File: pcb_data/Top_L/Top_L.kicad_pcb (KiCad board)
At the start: 2 copper layers, 134.5 x 96.4 mm, 42 parts, among them J1 Conn_01x02, U1 XIAO-nRF52840

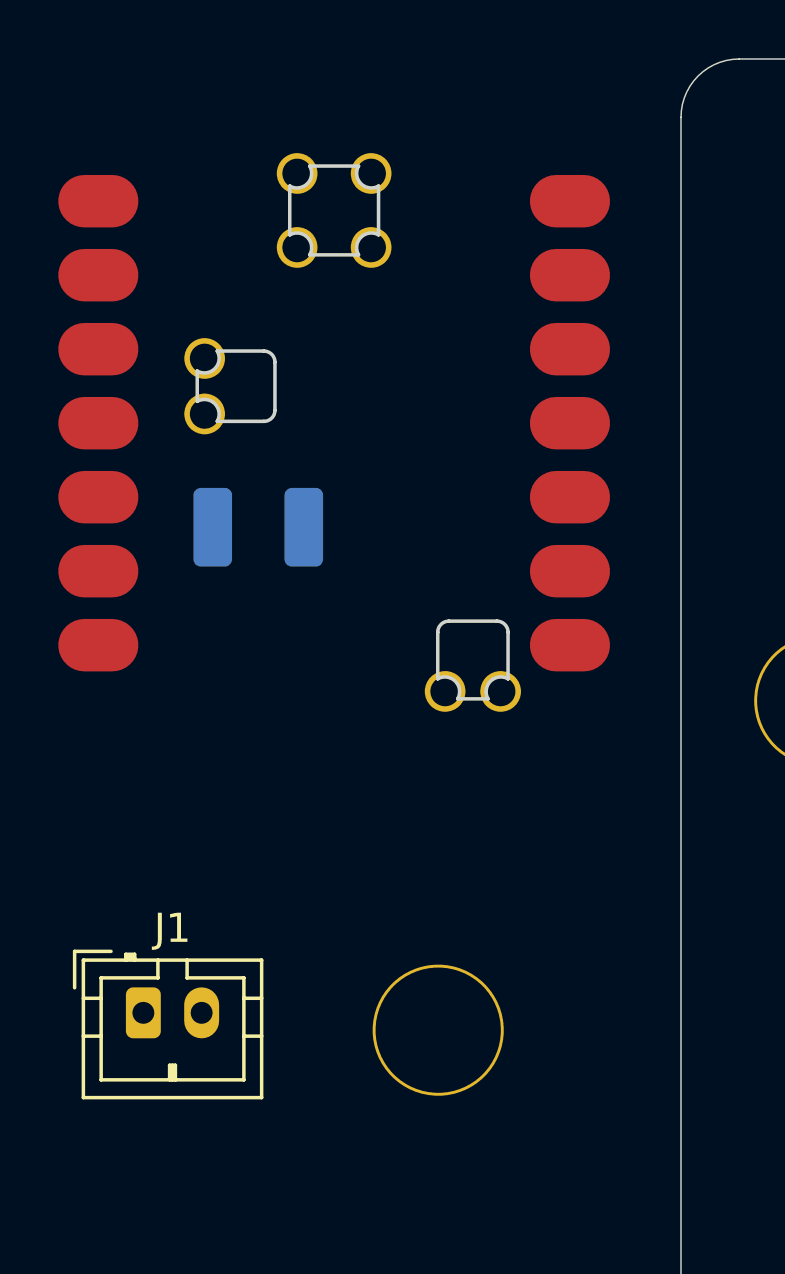
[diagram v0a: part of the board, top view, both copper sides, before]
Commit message: remove unnecessary footprint
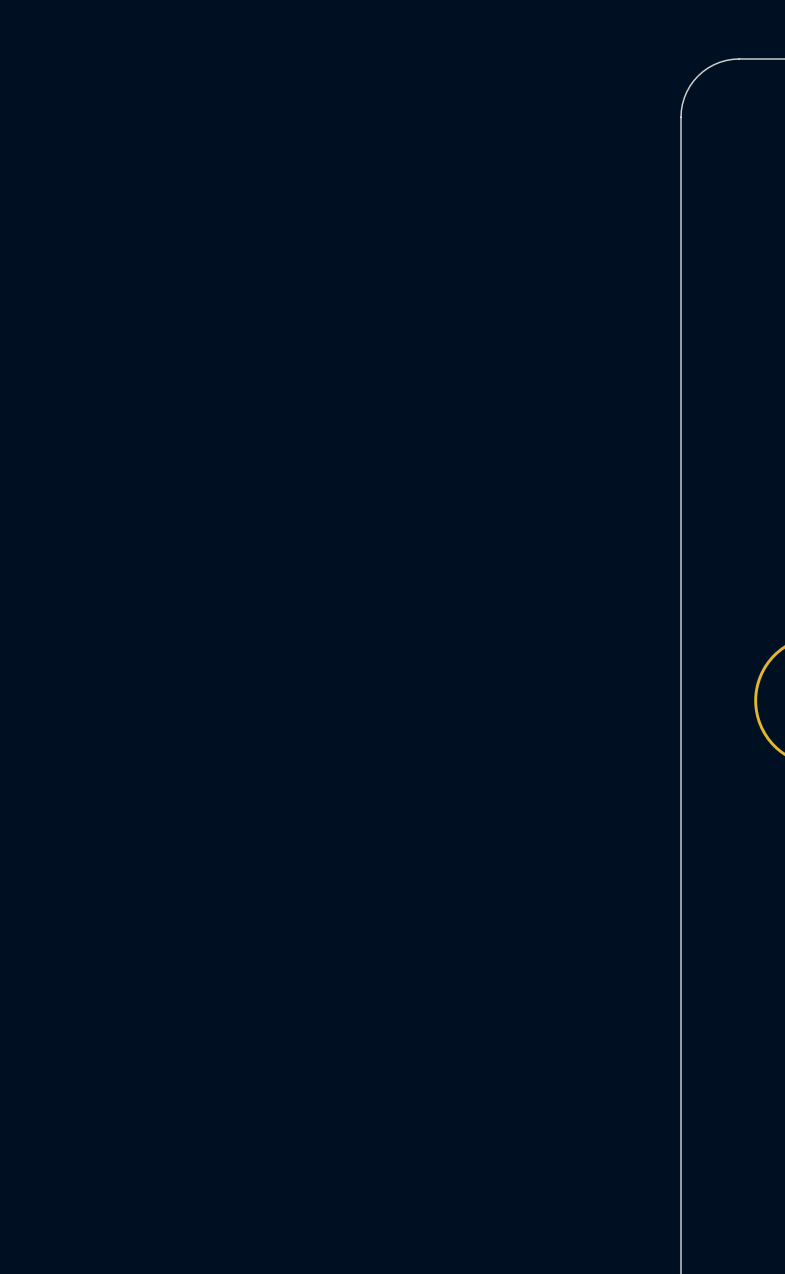
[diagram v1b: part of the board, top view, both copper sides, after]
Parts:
- removed C1: GRM32EC81C476KE15L, Capacitor_SMD:C_1210_3225Metric_Pad1.33x2.70mm_HandSolder
- removed H7: MountingHole, kbd_Hole:m2_Spacer_Hole
- removed J1: Conn_01x02, Connector_JST:JST_PH_B2B-PH-K_1x02_P2.00mm_Vertical
- removed U1: XIAO-nRF52840, mcu:xiao-ble-smd-cutout

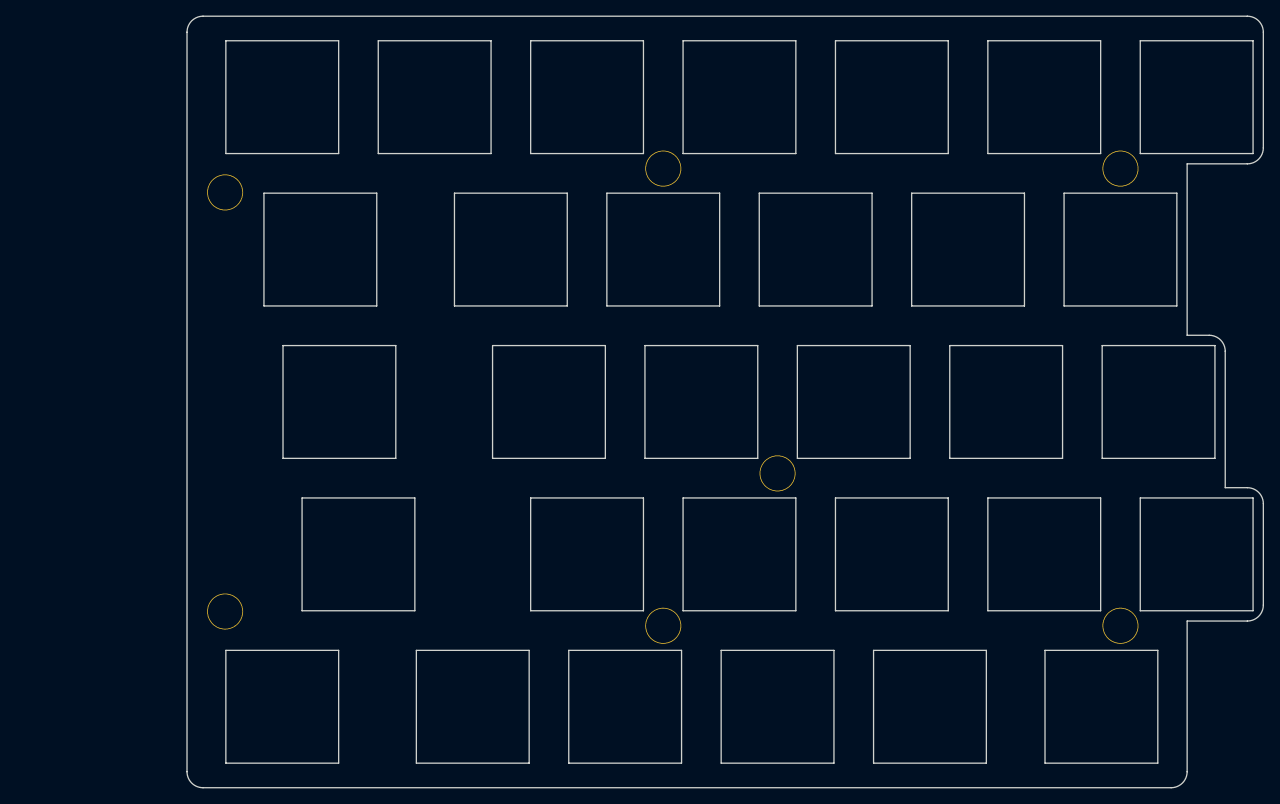
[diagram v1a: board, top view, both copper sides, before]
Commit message: fix hole footprint and number
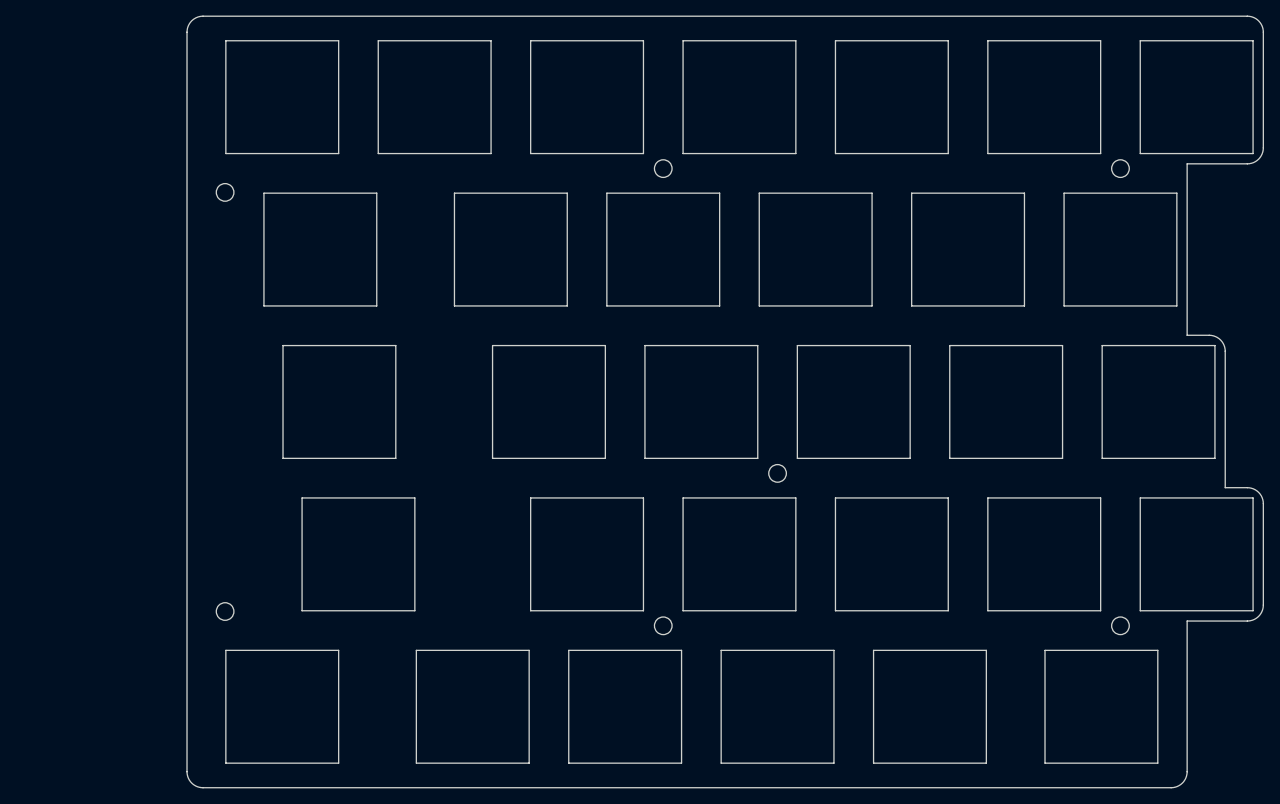
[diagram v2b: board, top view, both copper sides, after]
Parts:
- H1, H2, H3, H4, H5, H6: footprint kbd_Hole:m2_Spacer_Hole -> kbd_Hole:m2_Screw_Hole
- H7: renamed from H8; footprint kbd_Hole:m2_Spacer_Hole -> kbd_Hole:m2_Screw_Hole
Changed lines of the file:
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@@
 	)
 	(net 0 "")
-	(footprint "kbd_Hole:m2_Spacer_Hole"
+	(footprint "kbd_Hole:m2_Screw_Hole"
 		(layer "F.Cu")
 		(at 185.737656 66.079743)
@@
 			)
 		)
-		(property "Datasheet" "~"
+		(property "Datasheet" ""
 			(at 0 0 0)
 			(layer "F.Fab")
@@
 			)
 		)
-		(property "Description" "Mounting Hole without connection"
+		(property "Description" ""
 			(at 0 0 0)
 			(layer "F.Fab")
@@
 		(fp_circle
 			(center 0 0)
-			(end 2.3 0)
+			(end 2.45 0)
 			(stroke
 				(width 0.05)
@@
 		(pad "" np_thru_hole circle
 			(at 0 0)
-			(size 4.5 4.5)
-			(drill 4.3)
+			(size 2.2 2.2)
+			(drill 2.2)
 			(layers "*.Cu" "*.Mask")
 		)
 		(embedded_fonts no)
 	)
-	(footprint "kbd_Hole:m2_Spacer_Hole"
+	(footprint "kbd_Hole:m2_Screw_Hole"
 		(layer "F.Cu")
 		(at 185.737656 123.229791)
@@
 			)
 		)
-		(property "Datasheet" "~"
+		(property "Datasheet" ""
 			(at 0 0 0)
 			(layer "F.Fab")
@@
 			)
 		)
-		(property "Description" "Mounting Hole without connection"
+		(property "Description" ""
 			(at 0 0 0)
 			(layer "F.Fab")
@@
 		(fp_circle
 			(center 0 0)
-			(end 2.3 0)
+			(end 2.45 0)
 			(stroke
 				(width 0.05)
@@
 		(pad "" np_thru_hole circle
 			(at 0 0)
-			(size 4.5 4.5)
-			(drill 4.3)
+			(size 2.2 2.2)
+			(drill 2.2)
 			(layers "*.Cu" "*.Mask")
 		)
 		(embedded_fonts no)
 	)
-	(footprint "kbd_Hole:m2_Spacer_Hole"
+	(footprint "kbd_Hole:m2_Screw_Hole"
 		(layer "F.Cu")
 		(at 73.818812 69.056308)
@@
 			)
 		)
-		(property "Datasheet" "~"
+		(property "Datasheet" ""
 			(at 0 0 0)
 			(layer "F.Fab")
@@
 			)
 		)
-		(property "Description" "Mounting Hole without connection"
+		(property "Description" ""
 			(at 0 0 0)
 			(layer "F.Fab")
@@
 		(fp_circle
 			(center 0 0)
-			(end 2.3 0)
+			(end 2.45 0)
 			(stroke
 				(width 0.05)
@@
 		(pad "" np_thru_hole circle
 			(at 0 0)
-			(size 4.5 4.5)
-			(drill 4.3)
+			(size 2.2 2.2)
+			(drill 2.2)
 			(layers "*.Cu" "*.Mask")
 		)
 		(embedded_fonts no)
 	)
-	(footprint "kbd_Hole:m2_Spacer_Hole"
+	(footprint "kbd_Hole:m2_Screw_Hole"
 		(layer "F.Cu")
 		(at 128.587608 123.229791)
@@
 			)
 		)
-		(property "Datasheet" "~"
+		(property "Datasheet" ""
 			(at 0 0 0)
 			(layer "F.Fab")
@@
 			)
 		)
-		(property "Description" "Mounting Hole without connection"
+		(property "Description" ""
 			(at 0 0 0)
 			(layer "F.Fab")
@@
 		(fp_circle
 			(center 0 0)
-			(end 2.3 0)
+			(end 2.45 0)
 			(stroke
 				(width 0.05)
@@
 		(pad "" np_thru_hole circle
 			(at 0 0)
-			(size 4.5 4.5)
-			(drill 4.3)
+			(size 2.2 2.2)
+			(drill 2.2)
 			(layers "*.Cu" "*.Mask")
 		)
@@
 		(embedded_fonts no)
 	)
-	(footprint "kbd_Hole:m2_Spacer_Hole"
+	(footprint "kbd_Hole:m2_Screw_Hole"
 		(layer "F.Cu")
 		(at 142.87512 104.179775)
 		(descr "Mounting Hole 2.2mm, no annular, M2")
 		(tags "mounting hole 2.2mm no annular m2")
-		(property "Reference" "H8"
+		(property "Reference" "H7"
 			(at 0 -3.2 0)
 			(layer "F.Fab")
@@
 			)
 		)
-		(property "Datasheet" "~"
+		(property "Datasheet" ""
 			(at 0 0 0)
 			(layer "F.Fab")
@@
 			)
 		)
-		(property "Description" "Mounting Hole without connection"
+		(property "Description" ""
 			(at 0 0 0)
 			(layer "F.Fab")
@@
 		(fp_circle
 			(center 0 0)
-			(end 2.3 0)
+			(end 2.45 0)
 			(stroke
 				(width 0.05)
@@
 		(pad "" np_thru_hole circle
 			(at 0 0)
-			(size 4.5 4.5)
-			(drill 4.3)
+			(size 2.2 2.2)
+			(drill 2.2)
 			(layers "*.Cu" "*.Mask")
 		)
@@
 		(embedded_fonts no)
 	)
-	(footprint "kbd_Hole:m2_Spacer_Hole"
+	(footprint "kbd_Hole:m2_Screw_Hole"
 		(layer "F.Cu")
 		(at 128.587608 66.079743)
@@
 			)
 		)
-		(property "Datasheet" "~"
+		(property "Datasheet" ""
 			(at 0 0 0)
 			(layer "F.Fab")
@@
 			)
 		)
-		(property "Description" "Mounting Hole without connection"
+		(property "Description" ""
 			(at 0 0 0)
 			(layer "F.Fab")
@@
 		(fp_circle
 			(center 0 0)
-			(end 2.3 0)
+			(end 2.45 0)
 			(stroke
 				(width 0.05)
@@
 		(pad "" np_thru_hole circle
 			(at 0 0)
-			(size 4.5 4.5)
-			(drill 4.3)
+			(size 2.2 2.2)
+			(drill 2.2)
 			(layers "*.Cu" "*.Mask")
 		)
@@
 		(embedded_fonts no)
 	)
-	(footprint "kbd_Hole:m2_Spacer_Hole"
+	(footprint "kbd_Hole:m2_Screw_Hole"
 		(layer "F.Cu")
 		(at 73.818812 121.443852)
@@
 			)
 		)
-		(property "Datasheet" "~"
+		(property "Datasheet" ""
 			(at 0 0 0)
 			(layer "F.Fab")
@@
 			)
 		)
-		(property "Description" "Mounting Hole without connection"
+		(property "Description" ""
 			(at 0 0 0)
 			(layer "F.Fab")
@@
 		(fp_circle
 			(center 0 0)
-			(end 2.3 0)
+			(end 2.45 0)
 			(stroke
 				(width 0.05)
@@
 		(pad "" np_thru_hole circle
 			(at 0 0)
-			(size 4.5 4.5)
-			(drill 4.3)
+			(size 2.2 2.2)
+			(drill 2.2)
 			(layers "*.Cu" "*.Mask")
 		)
